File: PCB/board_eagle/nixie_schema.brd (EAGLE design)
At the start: 200 x 160 mm, 93 parts, among them Q1 BC856B, Q2 IRF740S, U2 MC7940N

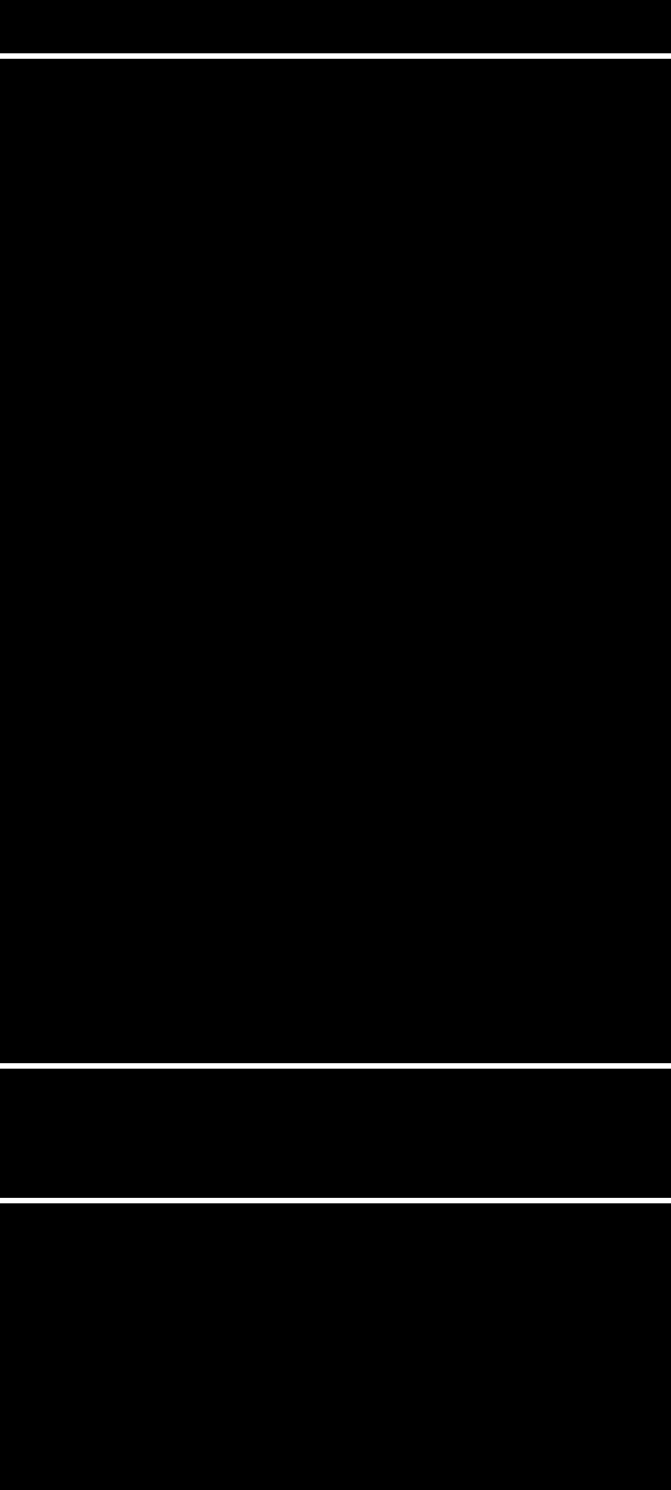
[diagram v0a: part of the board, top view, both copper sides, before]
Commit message: Added some footprints
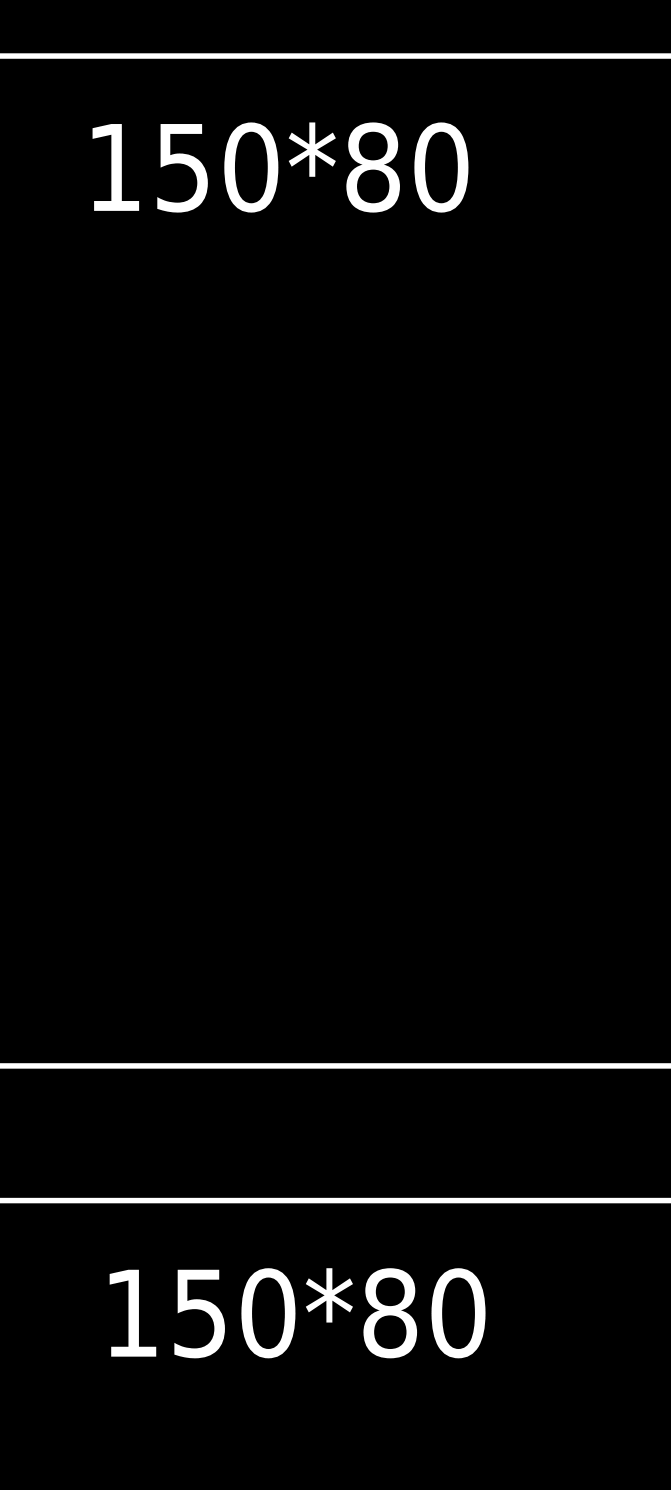
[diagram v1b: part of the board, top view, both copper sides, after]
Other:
- board text added: "150*80"
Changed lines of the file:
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@@
 <hole x="190" y="-75" drill="3.2"/>
 <hole x="10" y="-75" drill="3.2"/>
+<text x="85.09" y="-21.59" size="6.4516" layer="20">150*80</text>
+<text x="83.82" y="63.5" size="6.4516" layer="20">150*80</text>
 </plain>
 <attributes>

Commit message: Rebuilt boards
Boards are in the correct 150*80 format. repositioned b2b connectors
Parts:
- moved J1 262.5 mm to (-188.9, 40.9)
- moved U1 167.4 mm to (75.5, 13.1), turned to 90 degrees
- moved SV10 54.2 mm to (86.0, -30.0), turned to 90 degrees
- moved SV4 54.0 mm to (86.0, 60.0), turned to 90 degrees
- moved SV11 46.3 mm to (114.0, -30.0), turned to 90 degrees
- moved N5 46.1 mm to (114.0, -50.0)
- moved SV5 46.0 mm to (114.0, 60.0), turned to 90 degrees
- moved SV12 44.3 mm to (136.0, -30.0), turned to 90 degrees
- moved N6 44.1 mm to (136.0, -50.0)
- moved SV6 44.0 mm to (136.0, 60.0), turned to 90 degrees
- moved U$2 30.1 mm to (130.0, 30.0)
- moved N3 26.1 mm to (64.0, -50.0)
- moved N4 24.1 mm to (86.0, -50.0)
- moved U$1 20.2 mm to (20.0, 30.0)
- moved SV7 7.81 mm to (14.0, -30.0), turned to 90 degrees
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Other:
- board size 200 x 160 mm -> 150 x 170 mm
- board text added: "Rebuilt boards with new format"
- board text removed: "150*80"

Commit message: Added some more component footprints
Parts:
- removed G1: CR2032H, battery:CR2032H
- added BAT1: CR2032, nixe_cmp:CR2032
- added D4: B230A-13-F, nixe_cmp:SMA/SMB
- added J2: RTC_CONSMD, nixe_cmp:PICOBLADE_SMD_2
- added J4: RTC_CONTHT, nixe_cmp:PICOBLADE_THT_2
- added J5: (no value), con-jack:SPC4077
- D3: value (none) -> B230A-13-F; device diode:SOD123 -> nixe_cmp:SMA/SMB
- Y1: value (none) -> ECS-.327-7-34B; device crystal:SM49 -> nixe_cmp:CRYSTAL_PACK
- moved D3 165.1 mm to (-202.0, -219.5)
- moved Y1 112.9 mm to (-192.0, -162.0)
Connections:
- new net +: BAT1.+_2
- new net N$93: D4.A, J5.3
- net GND: now also BAT1.-, J2.-, J4.-, J5.1, J5.2; no longer G1.-
- net N$100: now also Y1.P$1; no longer Y1.2
- net N$22: now also BAT1.+_1, J2.+, J4.+; no longer G1.+
- net N$99: now also Y1.P$2; no longer Y1.1
- net VCC: now also D4.C

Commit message: Starting to do layout
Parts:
- C2: device rcl:140CLH-0810 -> rcl:C0805
- S1, S2, S3, S4, S5, S6: value TAC_SWITCHSMD -> (none); device SparkFun-Retired:TACTILE-SWITCH-SMD -> switch-omron:B3F-31XX
- moved J5 382.6 mm to (29.0, 69.0), turned to 270 degrees
- moved D4 369.8 mm to (26.9, 63.4)
- moved C3 352.2 mm to (144.0, 21.2)
- moved S6 265.6 mm to (100.0, 76.0), turned to 180 degrees
- moved S5 254.1 mm to (90.0, 76.0), turned to 180 degrees
- moved R28 250.4 mm to (86.0, 96.6)
- moved R29 250.4 mm to (86.0, 91.5)
- moved R30 250.4 mm to (86.0, 86.4)
- moved R7 250.4 mm to (86.0, 101.7)
- moved C1 245.4 mm to (34.5, 17.1)
- moved S4 242.8 mm to (80.0, 76.0), turned to 180 degrees
- moved S3 231.4 mm to (70.0, 76.0), turned to 180 degrees
- moved C10 223.7 mm to (-8.54, 26.2)
- moved S2 220.2 mm to (60.0, 76.0), turned to 180 degrees
- moved C14 216.9 mm to (-16.5, 32.0)
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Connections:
- net N$86 renamed V_PULSE
- new net N$94: SV7.11
- net +3V3: now also C7.1
- net BUTTON1: now also S3.2; no longer S2.3, S2.4
- net BUTTON2: now also S4.2; no longer S3.3, S3.4
- net BUTTON3: now also S5.2; no longer S4.3, S4.4
- net BUTTON4: now also S6.2; no longer S5.3, S5.4
- net GND: now also C1.2, C10.2, C11.2, C14.2, C2.2, C3.2, C4.2, C8.2, S6.1; no longer C2.-, S1.2, S2.2, S3.2, S4.2, S5.2, S6.3, S6.4
- net N$10: no longer SV7.11
- net N$12: now also C4.1
- net N$14: now also S1.2; no longer S1.3, S1.4
- net N$15: now also S2.2; no longer S6.1, S6.2
- net N$74: now also C10.1
- net N$96: now also C11.1
- net VCC: now also C1.1, C14.1, C2.1, C3.1, C8.1; no longer C2.+
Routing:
- net N$87: track 0.00 -> 22.0 mm
- net VCC: track 0.00 -> 14.6 mm
- net N$93: track 0.00 -> 2.75 mm
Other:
- board text added: "Anode resistors"
- board text added: "Button pullups"
- board text added: "ESP8266 stuff"
- board text added: "FRONT"
- board text added: "HV PSU stuff"
- board text added: "HV switches stuff"
- board text added: "LV PSU stuff"
- board text added: "RTC stuff"
- board text removed: "Rebuilt boards with new format"

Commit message: Some more routing
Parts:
- C12: device rcl:153CLV-0810 -> rcl:153CLV-1014
- moved C5 213.6 mm to (117.1, 41.0), turned to 90 degrees
- moved D3 208.8 mm to (95.9, 38.7), turned to 270 degrees
- moved C6 198.5 mm to (105.6, 41.0), turned to 90 degrees
- moved R9 195.8 mm to (80.5, 45.1)
- moved U$5 194.6 mm to (87.9, 47.0), turned to 90 degrees
- moved L1 194.0 mm to (84.6, 36.6), turned to 270 degrees
- moved R10 132.4 mm to (-31.6, 65.1)
- moved R32 132.3 mm to (-30.9, 60.2)
- moved C4 120.4 mm to (-21.0, 59.9)
- moved C8 120.4 mm to (-15.0, 61.8)
- moved D2 74.5 mm to (40.8, 35.5), turned to 270 degrees
- moved U$18 62.3 mm to (53.3, 41.7), turned to 270 degrees
- moved C13 52.4 mm to (41.2, 26.4), turned to 90 degrees
- moved C9 21.2 mm to (-18.9, -6.96)
- moved C1 16.3 mm to (22.5, 6.07)
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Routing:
- net VCC: track 14.6 -> 43.2 mm
- net N$13: track 0.00 -> 17.4 mm
- net N$5: track 0.00 -> 10.3 mm
- added copper zone on layer 1, net V_PULSE

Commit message: Routing the PCB
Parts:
- removed C2: 100n, rcl:C0805
- removed C9: 10u, rcl:140CLH-0810
- added P1: 100k, nixe_cmp:UNI_POT_SMD
- added R31, R33, R34, R35: 68k, rcl:R0603
- added R36: (no value), resistor:R0603
- added T1: (no value), nixe_cmp:C0805K
- J2: value RTC_CONSMD -> (none)
- J4: value RTC_CONTHT -> (none)
- R27: value 100k -> (none); device pot:SM-42/43X -> resistor:R0603
- Y1: value ECS-.327-7-34B -> (none)
- moved J2 291.8 mm to (147.0, 29.4), turned to 90 degrees
- moved J4 288.7 mm to (145.0, 36.9), turned to 90 degrees
- moved C16 267.0 mm to (94.0, 32.3), turned to 180 degrees
- moved C7 262.5 mm to (108.4, 30.2), turned to 270 degrees
- moved Y1 260.0 mm to (97.4, 30.9), turned to 90 degrees
- moved C15 258.5 mm to (94.0, 30.0), turned to 180 degrees
- moved R20 246.2 mm to (140.5, 52.5), turned to 270 degrees
- moved U2 238.6 mm to (102.5, 29.5)
- moved BAT1 231.6 mm to (99.9, 11.5)
- moved R19 223.6 mm to (118.5, 52.5), turned to 270 degrees
- moved R18 195.2 mm to (90.5, 52.5), turned to 270 degrees
- moved J3 190.1 mm to (147.7, 54.6), turned to 270 degrees
- moved R2 181.6 mm to (61.5, 20.7), turned to 180 degrees
- moved R17 172.6 mm to (68.5, 52.5), turned to 270 degrees
- moved R5 163.7 mm to (61.5, 25.8), turned to 180 degrees
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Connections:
- net N$1 renamed HV_DATA_IN
- net N$2 renamed HV_LE
- net N$6 renamed HV_DATA_CLK
- net N$7 renamed HV_DATA_OUT
- new net HV_HA_DP: R31.2, U$1.21
- new net HV_HB_DP: R33.2, U$1.22
- new net HV_MA_DP: R34.2, U$2.21
- new net HV_MB_DP: R35.2, U$2.22
- new net N$101: N3.LHDP, SV9.11
- new net N$102: N4.LHDP, SV10.11
- new net N$104: N6.LHDP, SV12.11
- new net N$105: N5.LHDP, SV11.11
- new net N$106: R31.1, SV1.11
- new net N$108: R33.1, SV2.11
- new net N$110: R34.1, SV3.11
- new net N$112: R35.1, SV4.11
- new net N$86: N2.LHDP, SV8.11
- new net PHOTO: R27.2, T1.COL, U1.ADC
- net +3V3: now also R27.1; no longer C9.+
- net GND: now also P1.P$2, R36.2; no longer C2.2, C9.-, R27.2
- net HV_MA_8: now also U$1.19
- net HV_MA_9: now also U$1.20; no longer U$1.19
- net N$109: now also R36.1, T1.EMI; no longer U$1.20
- net N$11: no longer SV3.11
- net N$19: no longer SV8.11
- net N$21: no longer SV9.11
- net N$45: no longer SV12.11
- net N$8: no longer SV4.11
- net N$88: no longer SV10.11
- net N$89: no longer SV1.11
- net N$90: no longer SV2.11
- net N$91: no longer SV6.11
- net N$92: no longer SV5.11
- net N$94: now also N1.LHDP
- net N$97: now also P1.P$3; no longer R27.3
- net N$98: no longer SV11.11
- net VCC: no longer C2.1
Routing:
- net VCC: track 43.2 -> 254.9 mm, vias 0 -> 4
- net HV_IN+: track 0.00 -> 195.8 mm, vias 0 -> 4
- net HV_DATA_CLK: track 0.00 -> 183.7 mm, vias 0 -> 10
- net HV_LE: track 0.00 -> 171.2 mm, vias 0 -> 8
- net +3V3: track 0.00 -> 123.4 mm, vias 0 -> 2
- net HV_DATA_OUT: track 0.00 -> 102.4 mm, vias 0 -> 2
- net HV_DATA_IN: track 0.00 -> 98.4 mm, vias 0 -> 5
- net N$87: track 21.6 -> 106.2 mm, vias 0 -> 4
- net N$22: track 0.00 -> 40.8 mm, vias 0 -> 1
- net BUTTON4: track 0.00 -> 34.2 mm, vias 0 -> 2
- net PHOTO: track 0.00 -> 32.4 mm
- net BUTTON3: track 0.00 -> 31.6 mm, vias 0 -> 2
- net DATA_CLK: track 0.00 -> 30.2 mm
- net DATA_IN: track 0.00 -> 28.6 mm
- net GND: track 0.00 -> 23.6 mm
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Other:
- board text removed: "Anode resistors"
- board text removed: "Button pullups"
- board text removed: "ESP8266 stuff"
- board text removed: "HV PSU stuff"
- board text removed: "HV switches stuff"
- board text removed: "LV PSU stuff"
- board text removed: "RTC stuff"
